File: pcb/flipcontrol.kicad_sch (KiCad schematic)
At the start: 96 parts, among them J1 PJ-202A, J2 DOT_BOARD_1, J3 DOT_BOARD_2, J4 LED_STRIP, J5 DOT_BOARD_3, J6 RJMG163118101NR, J7 FTDI, Q2 Si2347DS-T1-GE3, Q3 MMBT3904, Q4 Si2347DS-T1-GE3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

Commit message: PCB layout
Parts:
- TP1: value COIL_DRIVE_SENSE -> Drive sense
- TP2: value COIL_DRIVE_IN -> Drive in
- TP3: value LED_IN -> LED in
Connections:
- net COL_ADVANCE_1: now also U3.5 (GPIO5/TOUCH5/ADC1_CH4); no longer U3.6 (GPIO6/TOUCH6/ADC1_CH5)
- net COL_ADVANCE_2: now also U3.12 (GPIO8/TOUCH8/ADC1_CH7/SUBSPICS1); no longer U3.22 (GPIO14/TOUCH14/ADC2_CH3/FSPIWP/FSPIDQS/SUBSPIWP)
- net COL_ADVANCE_3: now also U3.23 (GPIO21); no longer U3.31 (GPIO38/FSPIWP/SUBSPIWP)
- net ENABLE_1: now also U3.18 (GPIO10/TOUCH10/ADC1_CH9/FSPICS0/FSPIIO4/SUBSPICS0); no longer U3.12 (GPIO8/TOUCH8/ADC1_CH7/SUBSPICS1)
- net ENABLE_2: now also U3.19 (GPIO11/TOUCH11/ADC2_CH0/FSPID/FSPIIO5/SUBSPID); no longer U3.17 (GPIO9/TOUCH9/ADC1_CH8/FSPIHD/SUBSPIHD)
- net ENABLE_3: now also U3.20 (GPIO12/TOUCH12/ADC2_CH1/FSPICLK/FSPIIO6/SUBSPICLK); no longer U3.18 (GPIO10/TOUCH10/ADC1_CH9/FSPICS0/FSPIIO4/SUBSPICS0)
- net ENABLE_4: now also U3.21 (GPIO13/TOUCH13/ADC2_CH2/FSPIQ/FSPIIO7/SUBSPIQ); no longer U3.19 (GPIO11/TOUCH11/ADC2_CH0/FSPID/FSPIIO5/SUBSPID)
- net ESP_LED: now also U3.31 (GPIO38/FSPIWP/SUBSPIWP); no longer U3.25 (GPIO48/SPICLK_N/SUBSPICLK_N_DIFF)
- net RESET_1: now also U3.4 (GPIO4/TOUCH4/ADC1_CH3); no longer U3.7 (GPIO7/TOUCH7/ADC1_CH6)
- net RESET_2: now also U3.17 (GPIO9/TOUCH9/ADC1_CH8/FSPIHD/SUBSPIHD); no longer U3.10 (GPIO17/U1TXD/ADC2_CH6)
- net RESET_3: now also U3.22 (GPIO14/TOUCH14/ADC2_CH3/FSPIWP/FSPIDQS/SUBSPIWP); no longer U3.24 (GPIO47/SPICLK_P/SUBSPICLK_P_DIFF)
- net ROW_ADVANCE_1: now also U3.6 (GPIO6/TOUCH6/ADC1_CH5); no longer U3.5 (GPIO5/TOUCH5/ADC1_CH4)
- net ROW_ADVANCE_2: now also U3.11 (GPIO18/U1RXD/ADC2_CH7/CLK_OUT3); no longer U3.21 (GPIO13/TOUCH13/ADC2_CH2/FSPIQ/FSPIIO7/SUBSPIQ)
- net ROW_ADVANCE_3: now also U3.24 (GPIO47/SPICLK_P/SUBSPICLK_P_DIFF); no longer U3.23 (GPIO21)
- net SET_UNSET_1: now also U3.7 (GPIO7/TOUCH7/ADC1_CH6); no longer U3.4 (GPIO4/TOUCH4/ADC1_CH3)
- net SET_UNSET_2: now also U3.10 (GPIO17/U1TXD/ADC2_CH6); no longer U3.20 (GPIO12/TOUCH12/ADC2_CH1/FSPICLK/FSPIIO6/SUBSPICLK)
- net SET_UNSET_3: now also U3.25 (GPIO48/SPICLK_N/SUBSPICLK_N_DIFF); no longer U3.11 (GPIO18/U1RXD/ADC2_CH7/CLK_OUT3)
- net ETH_TXN: now reaches R14.1, R15.2, U5.1 (TXN)
- net ETH_RXP: now reaches R12.2, R18.1, U5.6 (RXP)
- net ETH_RXN: now reaches R11.1, R19.1, U5.5 (RXN)
- net ETH_TXP: now reaches R13.1, R16.2, U5.2 (TXP)
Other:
- moved on the sheet: C10, C11, C12, C13, J6, R11, R12, R13, R14, R15, R16, R17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

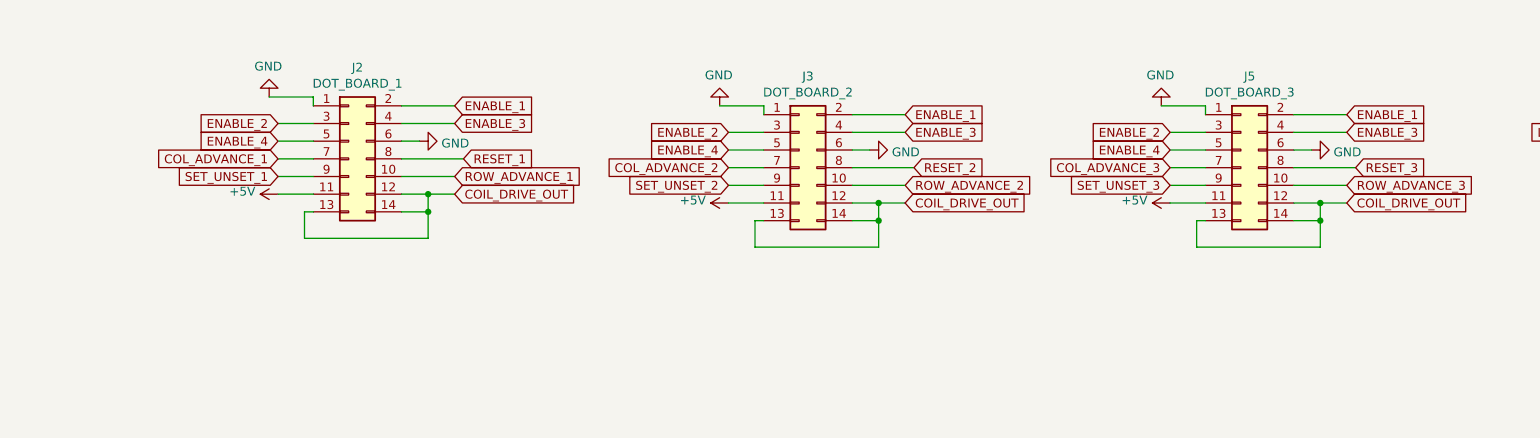
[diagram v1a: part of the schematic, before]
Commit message: Make panel pin 14 constantly powered with 18V
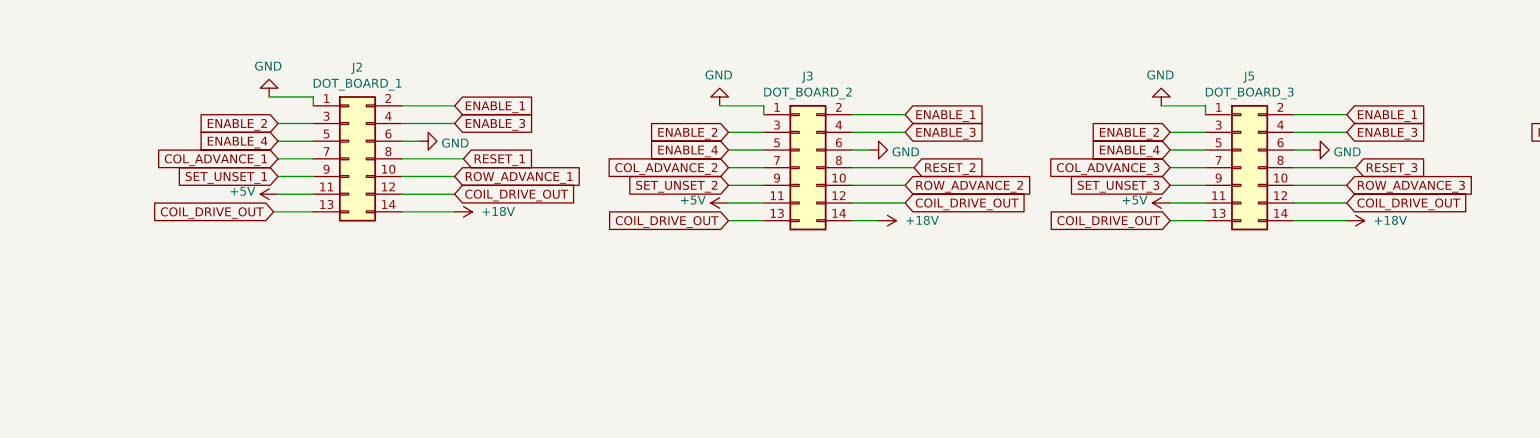
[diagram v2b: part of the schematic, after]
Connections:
- net +18V: now also J2.14 (Pin_14), J3.14 (Pin_14), J5.14 (Pin_14)
- net COIL_DRIVE_OUT: no longer J2.14 (Pin_14), J3.14 (Pin_14), J5.14 (Pin_14)
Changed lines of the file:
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@@
   (junction (at 379.095 281.94) (diameter 0) (color 0 0 0 0)
   )
-  (junction (at 347.98 179.07) (diameter 0) (color 0 0 0 0)
-  )
   (junction (at 66.04 224.155) (diameter 0) (color 0 0 0 0)
   )
@@
   (junction (at 89.535 190.5) (diameter 0) (color 0 0 0 0)
   )
-  (junction (at 283.21 177.8) (diameter 0) (color 0 0 0 0)
-  )
   (junction (at 502.92 207.645) (diameter 0) (color 0 0 0 0)
   )
   (junction (at 40.64 259.08) (diameter 0) (color 0 0 0 0)
   )
-  (junction (at 411.48 179.07) (diameter 0) (color 0 0 0 0)
-  )
   (junction (at 269.875 381) (diameter 0) (color 0 0 0 0)
   )
-  (junction (at 283.21 180.34) (diameter 0) (color 0 0 0 0)
-  )
   (junction (at 317.5 322.58) (diameter 0) (color 0 0 0 0)
   )
@@
   (junction (at 372.11 39.37) (diameter 0) (color 0 0 0 0)
   )
-  (junction (at 411.48 181.61) (diameter 0) (color 0 0 0 0)
-  )
   (junction (at 33.02 259.08) (diameter 0) (color 0 0 0 0)
   )
@@
   (junction (at 300.355 279.4) (diameter 0) (color 0 0 0 0)
   )
-  (junction (at 347.98 181.61) (diameter 0) (color 0 0 0 0)
-  )
   (junction (at 55.88 43.18) (diameter 0) (color 0 0 0 0)
   )
@@
     (stroke (width 0) (type default))
   )
-  (wire (pts (xy 279.4 177.8) (xy 283.21 177.8))
+  (wire (pts (xy 279.4 177.8) (xy 287.02 177.8))
     (stroke (width 0) (type default))
   )
@@
     (stroke (width 0) (type default))
   )
-  (wire (pts (xy 347.98 179.07) (xy 347.98 181.61))
-    (stroke (width 0) (type default))
-  )
   (wire (pts (xy 306.705 322.58) (xy 317.5 322.58))
     (stroke (width 0) (type default))
@@
     (stroke (width 0) (type default))
   )
-  (wire (pts (xy 407.67 179.07) (xy 411.48 179.07))
-    (stroke (width 0) (type default))
-  )
   (wire (pts (xy 66.04 224.155) (xy 72.39 224.155))
     (stroke (width 0) (type default))
@@
     (stroke (width 0) (type default))
   )
-  (wire (pts (xy 411.48 179.07) (xy 411.48 181.61))
-    (stroke (width 0) (type default))
-  )
   (wire (pts (xy 89.535 190.5) (xy 89.535 194.31))
     (stroke (width 0) (type default))
@@
     (stroke (width 0) (type default))
   )
-  (wire (pts (xy 266.7 180.34) (xy 265.43 180.34))
+  (wire (pts (xy 266.7 180.34) (xy 260.985 180.34))
     (stroke (width 0) (type default))
   )
@@
     (stroke (width 0) (type default))
   )
-  (wire (pts (xy 347.98 181.61) (xy 347.98 185.42))
-    (stroke (width 0) (type default))
-  )
   (wire (pts (xy 329.565 341.63) (xy 332.105 341.63))
     (stroke (width 0) (type default))
@@
     (stroke (width 0) (type default))
   )
-  (wire (pts (xy 283.21 180.34) (xy 283.21 184.15))
-    (stroke (width 0) (type default))
-  )
   (wire (pts (xy 387.985 339.09) (xy 387.985 345.44))
     (stroke (width 0) (type default))
@@
     (stroke (width 0) (type default))
   )
-  (wire (pts (xy 265.43 184.15) (xy 283.21 184.15))
-    (stroke (width 0) (type default))
-  )
   (wire (pts (xy 318.135 355.6) (xy 348.615 355.6))
     (stroke (width 0) (type default))
@@
     (stroke (width 0) (type default))
   )
-  (wire (pts (xy 411.48 181.61) (xy 407.67 181.61))
+  (wire (pts (xy 415.29 181.61) (xy 407.67 181.61))
     (stroke (width 0) (type default))
   )
@@
     (stroke (width 0) (type default))
   )
-  (wire (pts (xy 283.21 177.8) (xy 283.21 180.34))
-    (stroke (width 0) (type default))
-  )
   (wire (pts (xy 43.18 88.9) (xy 48.26 88.9))
     (stroke (width 0) (type default))
@@
     (stroke (width 0) (type default))
   )
-  (wire (pts (xy 283.21 180.34) (xy 279.4 180.34))
+  (wire (pts (xy 287.02 180.34) (xy 279.4 180.34))
     (stroke (width 0) (type default))
   )
-  (wire (pts (xy 331.47 181.61) (xy 330.2 181.61))
+  (wire (pts (xy 326.39 181.61) (xy 331.47 181.61))
     (stroke (width 0) (type default))
   )
@@
     (stroke (width 0) (type default))
   )
-  (wire (pts (xy 283.21 177.8) (xy 287.02 177.8))
-    (stroke (width 0) (type default))
-  )
   (wire (pts (xy 261.62 167.64) (xy 266.7 167.64))
     (stroke (width 0) (type default))
@@
     (stroke (width 0) (type default))
   )
-  (wire (pts (xy 344.17 179.07) (xy 347.98 179.07))
+  (wire (pts (xy 344.17 179.07) (xy 351.79 179.07))
     (stroke (width 0) (type default))
   )
@@
     (stroke (width 0) (type default))
   )
-  (wire (pts (xy 265.43 180.34) (xy 265.43 184.15))
-    (stroke (width 0) (type default))
-  )
   (wire (pts (xy 275.59 368.3) (xy 275.59 371.475))
     (stroke (width 0) (type default))
   )
-  (wire (pts (xy 393.7 181.61) (xy 393.7 185.42))
-    (stroke (width 0) (type default))
-  )
   (wire (pts (xy 476.25 171.45) (xy 476.25 172.72))
     (stroke (width 0) (type default))
@@
     (stroke (width 0) (type default))
   )
-  (wire (pts (xy 330.2 185.42) (xy 347.98 185.42))
-    (stroke (width 0) (type default))
-  )
   (wire (pts (xy 217.17 347.98) (xy 212.09 347.98))
     (stroke (width 0) (type default))
@@
     (stroke (width 0) (type default))
   )
-  (wire (pts (xy 393.7 185.42) (xy 411.48 185.42))
-    (stroke (width 0) (type default))
-  )
   (wire (pts (xy 326.39 173.99) (xy 331.47 173.99))
     (stroke (width 0) (type default))
@@
     (stroke (width 0) (type default))
   )
-  (wire (pts (xy 394.97 181.61) (xy 393.7 181.61))
-    (stroke (width 0) (type default))
-  )
-  (wire (pts (xy 330.2 181.61) (xy 330.2 185.42))
+  (wire (pts (xy 389.89 181.61) (xy 394.97 181.61))
     (stroke (width 0) (type default))
   )
@@
     (stroke (width 0) (type default))
   )
-  (wire (pts (xy 347.98 179.07) (xy 351.79 179.07))
-    (stroke (width 0) (type default))
-  )
   (wire (pts (xy 89.535 137.795) (xy 133.985 137.795))
     (stroke (width 0) (type default))
   )
-  (wire (pts (xy 411.48 179.07) (xy 415.29 179.07))
+  (wire (pts (xy 407.67 179.07) (xy 415.29 179.07))
     (stroke (width 0) (type default))
   )
@@
     (stroke (width 0) (type default))
   )
-  (wire (pts (xy 411.48 181.61) (xy 411.48 185.42))
-    (stroke (width 0) (type default))
-  )
   (wire (pts (xy 104.14 222.885) (xy 106.68 222.885))
     (stroke (width 0) (type default))
@@
     )
   )
+  (global_label "COIL_DRIVE_OUT" (shape input) (at 326.39 181.61 180)
+    (effects (font (size 1.27 1.27)) (justify right))
+    (property "Intersheetrefs" "${INTERSHEET_REFS}" (at 326.39 181.61 0)
+      (effects (font (size 1.27 1.27)) hide)
+    )
+  )
   (global_label "RESET_2" (shape output) (at 186.69 82.55 0)
     (effects (font (size 1.27 1.27)) (justify left))
@@
     )
   )
+  (global_label "COIL_DRIVE_OUT" (shape input) (at 260.985 180.34 180)
+    (effects (font (size 1.27 1.27)) (justify right))
+    (property "Intersheetrefs" "${INTERSHEET_REFS}" (at 260.985 180.34 0)
+      (effects (font (size 1.27 1.27)) hide)
+    )
+  )
   (global_label "COIL_DRIVE_IN" (shape input) (at 180.975 144.145 180) (fields_autoplaced)
     (effects (font (size 1.27 1.27)) (justify right))
@@
     )
   )
+  (global_label "COIL_DRIVE_OUT" (shape input) (at 389.89 181.61 180)
+    (effects (font (size 1.27 1.27)) (justify right))
+    (property "Intersheetrefs" "${INTERSHEET_REFS}" (at 389.89 181.61 0)
+      (effects (font (size 1.27 1.27)) hide)
+    )
+  )
   (global_label "ETH_TXP" (shape output) (at 259.08 322.58 0) (fields_autoplaced)
     (effects (font (size 1.27 1.27)) (justify left))
@@
     )
   )
+  (symbol (lib_id "flipcontrol-rescue:+18V-power") (at 347.98 181.61 270) (unit 1)
+    (in_bom yes) (on_board yes) (dnp no)
+    (property "Reference" "#PWR069" (at 344.17 181.61 0)
+      (effects (font (size 1.27 1.27)) hide)
+    )
+    (property "Value" "+18V" (at 351.79 181.61 90)
+      (effects (font (size 1.27 1.27)) (justify left))
+    )
+    (property "Footprint" "" (at 347.98 181.61 0)
+      (effects (font (size 1.27 1.27)) hide)
+    )
+    (property "Datasheet" "" (at 347.98 181.61 0)
+      (effects (font (size 1.27 1.27)) hide)
+    )
+    (pin "1")
+    (instances
+      (project "flipcontrol"
+        (path "/b93c5162-cc1e-49fa-86a7-af3aaf04b5c2"
+          (reference "#PWR069") (unit 1)
+        )
+      )
+    )
+  )
   (symbol (lib_id "power:+3V3") (at 55.88 33.02 0) (unit 1)
     (in_bom yes) (on_board yes) (dnp no) (fields_autoplaced)
@@
     )
   )
+  (symbol (lib_id "flipcontrol-rescue:+18V-power") (at 287.02 180.34 270) (unit 1)
+    (in_bom yes) (on_board yes) (dnp no)
+    (property "Reference" "#PWR068" (at 283.21 180.34 0)
+      (effects (font (size 1.27 1.27)) hide)
+    )
+    (property "Value" "+18V" (at 290.83 180.34 90)
+      (effects (font (size 1.27 1.27)) (justify left))
+    )
+    (property "Footprint" "" (at 287.02 180.34 0)
+      (effects (font (size 1.27 1.27)) hide)
+    )
+    (property "Datasheet" "" (at 287.02 180.34 0)
+      (effects (font (size 1.27 1.27)) hide)
+    )
+    (pin "1")
+    (instances
+      (project "flipcontrol"
+        (path "/b93c5162-cc1e-49fa-86a7-af3aaf04b5c2"
+          (reference "#PWR068") (unit 1)
+        )
+      )
+    )
+  )
   (symbol (lib_id "Connector:Conn_01x06_Pin") (at 273.05 78.74 180) (unit 1)
     (in_bom yes) (on_board yes) (dnp no) (fields_autoplaced)
@@
         )
       )
+    )
+  )
+  (symbol (lib_id "flipcontrol-rescue:+18V-power") (at 415.29 181.61 270) (unit 1)
+    (in_bom yes) (on_board yes) (dnp no)
+    (property "Reference" "#PWR070" (at 411.48 181.61 0)
+      (effects (font (size 1.27 1.27)) hide)
+    )
+    (property "Value" "+18V" (at 419.1 181.61 90)
+      (effects (font (size 1.27 1.27)) (justify left))
+    )
+    (property "Footprint" "" (at 415.29 181.61 0)
+      (effects (font (size 1.27 1.27)) hide)
+    )
+    (property "Datasheet" "" (at 415.29 181.61 0)
+      (effects (font (size 1.27 1.27)) hide)
+    )
+    (pin "1")
+    (instances
+      (project "flipcontrol"
+        (path "/b93c5162-cc1e-49fa-86a7-af3aaf04b5c2"
+          (reference "#PWR070") (unit 1)
+        )
+      )
